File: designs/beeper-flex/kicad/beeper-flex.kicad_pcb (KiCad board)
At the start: 2 copper layers, 22 x 5.3 mm, 5 parts

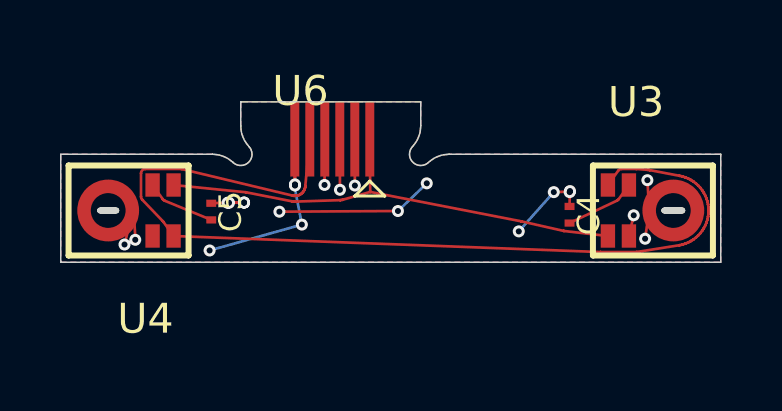
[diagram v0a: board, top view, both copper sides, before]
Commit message: vdd pour not rendering upon deleting extra gnd vias
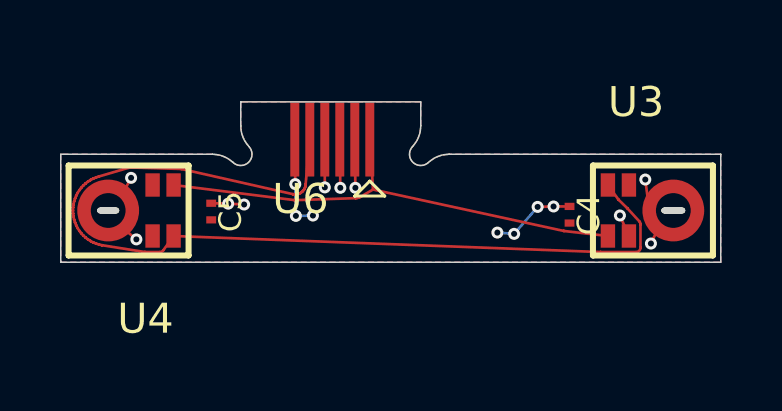
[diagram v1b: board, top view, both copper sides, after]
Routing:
- net VDDMIC: track 17.5 -> 3.13 mm, vias 7 -> 3
- net GND: track 14.1 -> 12.0 mm, vias 16 -> 14

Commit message: somewhat stable flex design
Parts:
- U3, U4: value ~ -> IM69D130V01XTSA1
- U6: value ~ -> Edge-FH19C-6S-0.5SH(10)
- moved U6 0.05 mm to (129.4, 100.0)
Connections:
- net PDM_clk renamed /PDM_clk
- net PDM_data renamed /PDM_data
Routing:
- net VDDMIC: track 3.13 -> 9.73 mm, vias 3 -> 6
- net GND: track 12.0 -> 12.4 mm, vias 14 -> 13
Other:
- net class Default removed

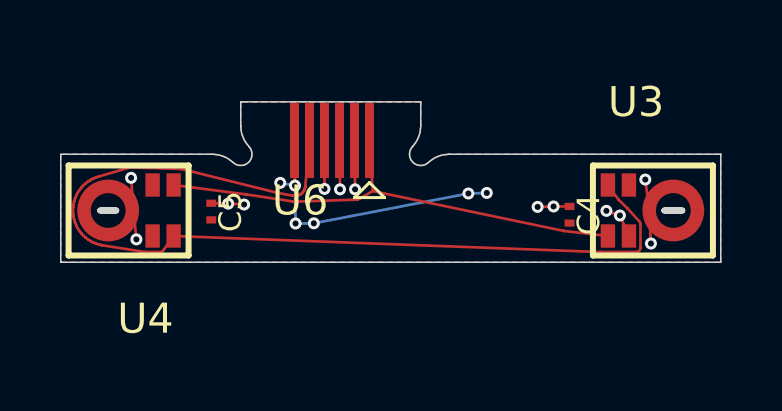
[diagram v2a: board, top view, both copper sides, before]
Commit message: experimenting with removing requires/supports
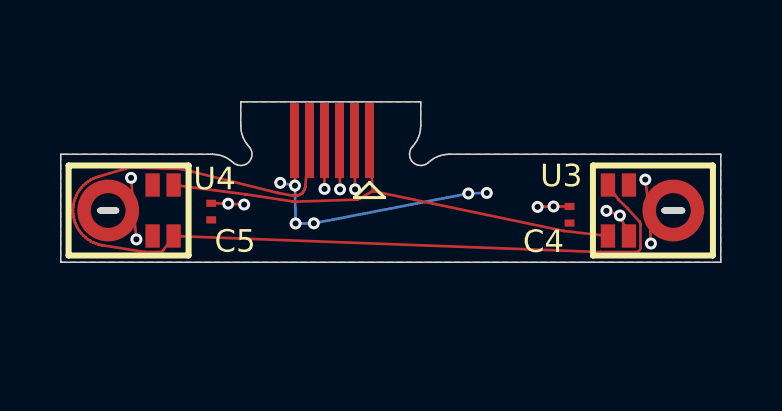
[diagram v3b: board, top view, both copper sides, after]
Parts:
- U3, U4: value IM69D130V01XTSA1 -> ~
- U6: value Edge-FH19C-6S-0.5SH(10) -> ~
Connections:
- net /PDM_clk renamed PDM_clk
- net /PDM_data renamed PDM_data
